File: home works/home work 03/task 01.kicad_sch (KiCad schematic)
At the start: 0 parts

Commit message: start home work 3. task 1
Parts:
- added D1: Wgite, symbol Device:LED
- added D10, D11, D12, D13, D14, D15, D16, D17, D18, D19, D2, D3, D4, D5, D6, D7, D8, D9: LED, symbol Device:LED
- added R1, R10, R2, R3, R4, R5, R6, R7, R8, R9: R, symbol Device:R
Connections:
- new net: D1.2 (A), R1.1
- new net: D18.1 (K), D19.2 (A)
- new net: D8.1 (K), D9.2 (A)
- new net: D8.2 (A), R5.1
- new net: D4.1 (K), D5.2 (A)
- new net: D12.1 (K), D13.2 (A)
- new net: D12.2 (A), R7.1
- new net: D10.2 (A), R6.1
- new net: D6.2 (A), R4.1
- new net: D16.1 (K), D17.2 (A)
- new net: D16.2 (A), R9.1
- new net: D6.1 (K), D7.2 (A)
- new net: D14.1 (K), D15.2 (A)
- new net: D4.2 (A), R3.1
- new net: D14.2 (A), R8.1
- new net: D10.1 (K), D11.2 (A)
- new net: D2.1 (K), D3.2 (A)
- new net: D2.2 (A), R2.1
- new net: D18.2 (A), R10.1
- new net +11V7: R2.2
- new net +12V7: R10.2, R3.2, R4.2, R5.2, R6.2, R7.2, R8.2, R9.2
- new net +7V4: R1.2
- new net GND: D1.1 (K), D11.1 (K), D13.1 (K), D15.1 (K), D17.1 (K), D19.1 (K), D3.1 (K), D5.1 (K), D7.1 (K), D9.1 (K)
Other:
- note added: "Задача 1 - Рассчитать номинал и мощность резистора для подключения одного белого светодиода к источнику напряжения 7,4 В. - Рассчитать номинал и мощность резистора для последовательного подключения двух зеленых светодиодов к источнику напряжения 11,7 В. - Рассчитать номинал и мощность резисторов для последовательно-параллельного подключения шестнадцати красных светодиодов к источнику напряжения 1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"

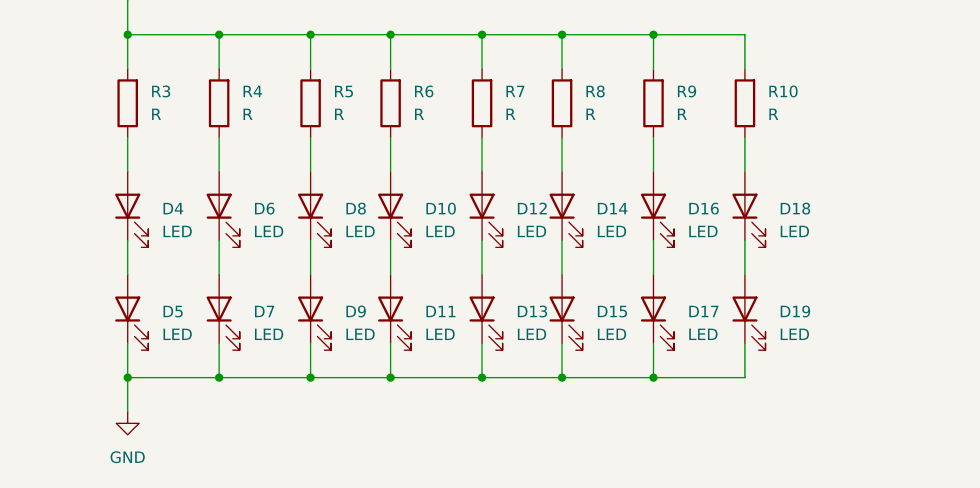
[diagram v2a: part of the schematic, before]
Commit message: fix led labesl to red
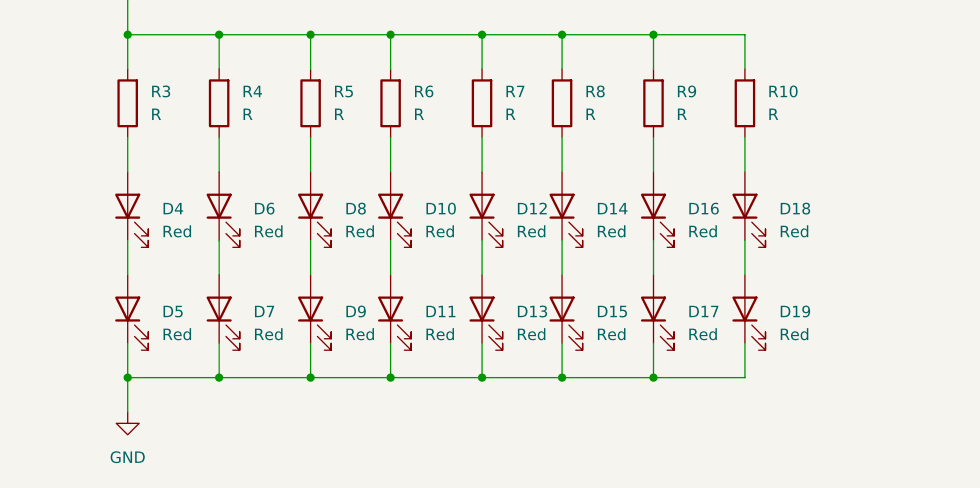
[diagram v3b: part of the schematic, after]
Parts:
- D10, D11, D12, D13, D14, D15, D16, D17, D18, D19, D4, D5, D6, D7, D8, D9: value LED -> Red

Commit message: home work 3
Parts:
- D2, D3: value LED -> Green
- R1: value R -> 91
- R10, R3, R4, R5, R6, R7, R8, R9: value R -> 150
- R2: value R -> 240
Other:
- note added: "U_{D1} = 3.2V I_{D1} = 0.05A U_{R1} = 7.4 - 3.2 = 4.4V R_{R1} = U_{R1} / I_{D1} = 4.4 / 0.05 = 88Ω → 91Ω P_{R1} = U_{R1} * I_{D1} = 4.4 * 0.05 = 0.22W → 0.25W"
- note added: "U_{D2..D3} = 2.1V I_{D2..D3} = 0.02A U_{R2} = 11.7 - 2.1 - 2.1 = 4.5V R_{R2} = U_{R2} / I_{D2..D3} = 4.5 / 0.02 = 225Ω → 240Ω P_{R2} = U_{R2} * I_{D2..D3} = 11.7 * 0.02 = 0.234W → 0.25W"
- note added: "U_{D4..D17} = 5V I_{D4..D17} = 0.02A U_{R3..R10} = 12.7 - 5 - 5 = 2.7V R_{R3..R10} = U_{R3..R10} / I_{D4..D17} = 2.7 / 0.02 = 135Ω → 150Ω P_{R2} = U_{R2} * I_{D2..D3} = 12.7 * 0.02 = 0.254W → 0.25W"
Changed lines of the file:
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@@
+		)
+	)
+	(text "U_{D2..D3} = 2.1V\nI_{D2..D3} = 0.02A\n\nU_{R2} = 11.7 - 2.1 - 2.1 = 4.5V\nR_{R2} =  U_{R2} / I_{D2..D3} = 4.5 / 0.02 = 225Ω → 240Ω\n\nP_{R2} = U_{R2} * I_{D2..D3} = 11.7 * 0.02 = 0.234W → 0.25W"
+		(exclude_from_sim no)
+		(at 138.43 74.676 0)
+		(effects
+			(font
+				(size 1.27 1.27)
+			)
+			(justify left)
 		)
 	)
@@
 		)
 	)
+	(text "U_{D1} = 3.2V\nI_{D1} = 0.05A\n\nU_{R1} = 7.4 - 3.2 = 4.4V\nR_{R1} = U_{R1} / I_{D1} = 4.4 / 0.05 = 88Ω → 91Ω\n\nP_{R1} = U_{R1} * I_{D1} = 4.4 * 0.05 = 0.22W → 0.25W"
+		(exclude_from_sim no)
+		(at 138.684 50.292 0)
+		(effects
+			(font
+				(size 1.27 1.27)
+			)
+			(justify left)
+		)
+	)
+	(text "U_{D4..D17} = 5V\nI_{D4..D17} = 0.02A\n\nU_{R3..R10} = 12.7 - 5 - 5 = 2.7V\nR_{R3..R10} = U_{R3..R10} / I_{D4..D17} = 2.7 / 0.02 = 135Ω → 150Ω\n\nP_{R2} = U_{R2} * I_{D2..D3} = 12.7 * 0.02 = 0.254W → 0.25W"
+		(exclude_from_sim no)
+		(at 138.938 104.394 0)
+		(effects
+			(font
+				(size 1.27 1.27)
+			)
+			(justify left)
+		)
+	)
 	(symbol
 		(lib_id "Device:R")
@@
 			)
 		)
-		(property "Value" "R"
+		(property "Value" "91"
 			(at 69.85 46.99 90)
 			(effects
@@
 			)
 		)
-		(property "Value" "R"
+		(property "Value" "150"
 			(at 74.93 106.6799 0)
 			(effects
@@
 			)
 		)
-		(property "Value" "R"
+		(property "Value" "150"
 			(at 83.82 106.6799 0)
 			(effects
@@
 			)
 		)
-		(property "Value" "R"
+		(property "Value" "150"
 			(at 64.77 106.6799 0)
 			(effects
@@
 			)
 		)
-		(property "Value" "LED"
+		(property "Value" "Green"
 			(at 89.2175 69.85 0)
 			(effects
@@
 			)
 		)
-		(property "Value" "R"
+		(property "Value" "150"
 			(at 113.03 106.6799 0)
 			(effects
@@
 			)
 		)
-		(property "Value" "R"
+		(property "Value" "150"
 			(at 102.87 106.6799 0)
 			(effects
@@
 			)
 		)
-		(property "Value" "LED"
+		(property "Value" "Green"
 			(at 77.7875 69.85 0)
 			(effects
@@
 			)
 		)
-		(property "Value" "R"
+		(property "Value" "150"
 			(at 123.19 106.6799 0)
 			(effects
@@
 			)
 		)
-		(property "Value" "R"
+		(property "Value" "150"
 			(at 54.61 106.6799 0)
 			(effects
@@
 			)
 		)
-		(property "Value" "R"
+		(property "Value" "150"
 			(at 93.98 106.6799 0)
 			(effects
@@
 			)
 		)
-		(property "Value" "R"
+		(property "Value" "240"
 			(at 64.77 71.12 90)
 			(effects

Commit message: home works 3 and 4
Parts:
- R1: value 91 -> 220
- R10, R3, R4, R5, R6, R7, R8, R9: value 150 -> 470
- R2: value 240 -> 390
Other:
- note added: "U_{D1} = 3.2V I_{D1} = 0.05A U_{R1} = 7.4 - 3.2 = 4.2V R_{R1} = U_{R1} / I_{D1} = 4.2 / 0.02 = 210Ω → 220Ω P_{R1} = U_{R1} * I_{D1} = 4.2 * 0.02 = 0.084W → 0.125W или 0603"
- note added: "U_{D2..D3} = 2.1V I_{D2..D3} = 0.02A U_{R2} = 11.7 - 2.1 - 2.1 = 7.5V R_{R2} = U_{R2} / I_{D2..D3} = 7.5 / 0.02 = 375Ω → 390Ω P_{R2} = U_{R2} * I_{D2..D3} = 11.7 * 0.02 = 0.234W → 0.25W"
- note added: "U_{D4..D19} = 5V I_{D4..D19} = 0.02A U_{R3..R10} = 12.7 - 2 - 2 = 8.7V R_{R3..R10} = U_{R3..R10} / I_{D4..D19} = 8.7 / 0.02 = 435Ω → 470Ω P_{R3} = U_{R3} * I_{D2..D3} = 12.7 * 0.02 = 0.254W → 0.25W"
- note removed: "U_{D1} = 3.2V I_{D1} = 0.05A U_{R1} = 7.4 - 3.2 = 4.4V R_{R1} = U_{R1} / I_{D1} = 4.4 / 0.05 = 88Ω → 91Ω P_{R1} = U_{R1} * I_{D1} = 4.4 * 0.05 = 0.22W → 0.25W"
- note removed: "U_{D2..D3} = 2.1V I_{D2..D3} = 0.02A U_{R2} = 11.7 - 2.1 - 2.1 = 4.5V R_{R2} = U_{R2} / I_{D2..D3} = 4.5 / 0.02 = 225Ω → 240Ω P_{R2} = U_{R2} * I_{D2..D3} = 11.7 * 0.02 = 0.234W → 0.25W"
- note removed: "U_{D4..D17} = 5V I_{D4..D17} = 0.02A U_{R3..R10} = 12.7 - 5 - 5 = 2.7V R_{R3..R10} = U_{R3..R10} / I_{D4..D17} = 2.7 / 0.02 = 135Ω → 150Ω P_{R2} = U_{R2} * I_{D2..D3} = 12.7 * 0.02 = 0.254W → 0.25W"
- moved on the sheet: D1, D10, D11, D12, D13, D14, D15, D16, D17, D18, D19, D2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
